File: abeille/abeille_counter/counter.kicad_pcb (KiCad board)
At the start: 2 copper layers, 3 parts, among them IC1 ATMEGA328-P

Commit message: start placing counter components
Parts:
- removed D1: LED, LEDs:LED-3MM
- removed IC1: ATMEGA328-P, Housings_DIP:DIP-28_W7.62mm_LongPads
- added P1: HE10-10, Connect:IDC_Header_Straight_10pins, B.Cu at (73.7, 108.0)
- added P2: HE10-10, Connect:IDC_Header_Straight_10pins, B.Cu at (212.1, 108.0)
- added R10: 100K, Resistors_SMD:R_1206_HandSoldering, F.Cu at (63.5, -96.5)
- added R11: 100K, Resistors_SMD:R_1206_HandSoldering, F.Cu at (63.5, -109.2)
- added R12: 100K, Resistors_SMD:R_1206_HandSoldering, F.Cu at (62.2, -123.2)
- added R13: 1K, Resistors_SMD:R_1206_HandSoldering, F.Cu at (62.2, -134.6)
- added R14: 1K, Resistors_SMD:R_1206_HandSoldering, F.Cu at (62.2, -144.8)
- added R15: 1K, Resistors_SMD:R_1206_HandSoldering, F.Cu at (174.0, 114.3)
- added R16: 1K, Resistors_SMD:R_1206_HandSoldering, F.Cu at (166.4, 114.3)
- added R17: 1K, Resistors_SMD:R_1206_HandSoldering, F.Cu at (110.5, 92.7)
- added R18: 1K, Resistors_SMD:R_1206_HandSoldering, F.Cu at (108.0, 114.3)
- added R19: 1K, Resistors_SMD:R_1206_HandSoldering, F.Cu at (94.0, -101.6)
- added R2: 1K, Resistors_SMD:R_1206_HandSoldering, F.Cu at (83.8, 113.0)
- added R20: 1K, Resistors_SMD:R_1206_HandSoldering, F.Cu at (94.0, -115.6)
- added R21: 100K, Resistors_SMD:R_1206_HandSoldering, F.Cu at (95.2, -128.3)
- added R22: 100K, Resistors_SMD:R_1206_HandSoldering, F.Cu at (95.2, -143.5)
- added R23: 100K, Resistors_SMD:R_1206_HandSoldering, F.Cu at (124.5, -143.5)
- added R24: 100K, Resistors_SMD:R_1206_HandSoldering, F.Cu at (124.5, -128.3)
- added R25: 1K, Resistors_SMD:R_1206_HandSoldering, F.Cu at (125.7, -115.6)
- added R26: 1K, Resistors_SMD:R_1206_HandSoldering, F.Cu at (127.0, -100.3)
- added R27: 1K, Resistors_SMD:R_1206_HandSoldering, F.Cu at (127.0, -87.6)
- added R28: 1K, Resistors_SMD:R_1206_HandSoldering, F.Cu at (127.0, -74.9)
- added R29: 1K, Resistors_SMD:R_1206_HandSoldering, F.Cu at (128.3, 91.4)
- added R3: 1K, Resistors_SMD:R_1206_HandSoldering, F.Cu at (95.2, -59.7)
- added R30: 1K, Resistors_SMD:R_1206_HandSoldering, F.Cu at (127.0, 114.3)
- added R31: 1K, Resistors_SMD:R_1206_HandSoldering, F.Cu at (194.3, 92.7)
- added R32: 1K, Resistors_SMD:R_1206_HandSoldering, F.Cu at (194.3, 113.0)
- added R33: 100K, Resistors_SMD:R_1206_HandSoldering, F.Cu at (149.9, -143.5)
- added R34: 100K, Resistors_SMD:R_1206_HandSoldering, F.Cu at (149.9, -127.0)
- added R35: 100K, Resistors_SMD:R_1206_HandSoldering, F.Cu at (149.9, -113.0)
- added R36: 100K, Resistors_SMD:R_1206_HandSoldering, F.Cu at (151.1, -97.8)
- added R37: 1K, Resistors_SMD:R_1206_HandSoldering, F.Cu at (152.4, -82.5)
- added R38: 1K, Resistors_SMD:R_1206_HandSoldering, F.Cu at (152.4, -66.0)
- added R39: 1K, Resistors_SMD:R_1206_HandSoldering, F.Cu at (201.9, 92.7)
- added R4: 1K, Resistors_SMD:R_1206_HandSoldering, F.Cu at (95.2, -76.2)
- added R40: 1K, Resistors_SMD:R_1206_HandSoldering, F.Cu at (186.7, 113.0)
- added R41: 1K, Resistors_SMD:R_1206_HandSoldering, F.Cu at (143.5, 91.4)
- added R42: 1K, Resistors_SMD:R_1206_HandSoldering, F.Cu at (143.5, 114.3)
- added R43: 1K, Resistors_SMD:R_1206_HandSoldering, F.Cu at (171.4, -144.8)
- added R44: 1K, Resistors_SMD:R_1206_HandSoldering, F.Cu at (171.4, -127.0)
- added R45: 100K, Resistors_SMD:R_1206_HandSoldering, F.Cu at (172.7, -114.3)
- added R46: 100K, Resistors_SMD:R_1206_HandSoldering, F.Cu at (172.7, -99.1)
- added R47: 100K, Resistors_SMD:R_1206_HandSoldering, F.Cu at (172.7, -83.8)
- added R48: 100K, Resistors_SMD:R_1206_HandSoldering, F.Cu at (172.7, -66.0)
- added R49: 0, Resistors_SMD:R_1206_HandSoldering, B.Cu at (86.4, 87.6)
- added R5: 1K, Resistors_SMD:R_1206_HandSoldering, F.Cu at (92.7, -90.2)
- added R50: 0, Resistors_SMD:R_1206_HandSoldering, B.Cu at (81.3, 87.6)
- added R51: 0, Resistors_SMD:R_1206_HandSoldering, B.Cu at (76.2, 87.6)
- added R52: 0, Resistors_SMD:R_1206_HandSoldering, B.Cu at (217.2, 120.7)
- added R53: 0, Resistors_SMD:R_1206_HandSoldering, F.Cu at (195.6, -143.5)
- added R54: 0, Resistors_SMD:R_1206_HandSoldering, F.Cu at (195.6, -128.3)
- added R55: 0, Resistors_SMD:R_1206_HandSoldering, F.Cu at (196.8, -114.3)
- added R56: 0, Resistors_SMD:R_1206_HandSoldering, F.Cu at (195.6, -100.3)
- added R57: 0, Resistors_SMD:R_1206_HandSoldering, F.Cu at (196.8, -82.5)
- added R6: 1K, Resistors_SMD:R_1206_HandSoldering, F.Cu at (61.0, -47.0)
- added R7: 1K, Resistors_SMD:R_1206_HandSoldering, F.Cu at (61.0, -58.4)
- added R8: 1K, Resistors_SMD:R_1206_HandSoldering, F.Cu at (63.5, -69.8)
- added R9: 100K, Resistors_SMD:R_1206_HandSoldering, F.Cu at (63.5, -83.8)
- added U1: IN_0, counter_footprint:ITR9608_DIP-4_0_ELL, F.Cu at (86.4, 99.1)
- added U10: OUT_2, counter_footprint:ITR9608_DIP-4_0_ELL, F.Cu at (119.4, 106.7)
- added U11: IN_6, counter_footprint:ITR9608_DIP-4_0_ELL, F.Cu at (185.4, 99.1)
- added U12: OUT_6, counter_footprint:ITR9608_DIP-4_0_ELL, F.Cu at (185.4, 106.7)
- added U13: IN_3, counter_footprint:ITR9608_DIP-4_0_ELL, F.Cu at (135.9, 99.1)
- added U14: OUT_3, counter_footprint:ITR9608_DIP-4_0_ELL, F.Cu at (135.9, 106.7)
- added U15: IN_7, counter_footprint:ITR9608_DIP-4_0_ELL, F.Cu at (201.9, 99.1)
- added U16: OUT_7, counter_footprint:ITR9608_DIP-4_0_ELL, F.Cu at (201.9, 106.7)
- added U17: pca9555, Housings_DIP:DIP-24_W15.24mm_LongPads, B.Cu at (130.8, 95.2)
- added U2: OUT_0, counter_footprint:ITR9608_DIP-4_0_ELL, F.Cu at (86.4, 106.7)
- added U3: IN_4, counter_footprint:ITR9608_DIP-4_0_ELL, F.Cu at (152.4, 99.1)
- added U4: OUT_4, counter_footprint:ITR9608_DIP-4_0_ELL, F.Cu at (152.4, 106.7)
- added U5: IN_1, counter_footprint:ITR9608_DIP-4_0_ELL, F.Cu at (102.9, 99.1)
- added U6: OUT_1, counter_footprint:ITR9608_DIP-4_0_ELL, F.Cu at (102.9, 106.7)
- added U7: IN_5, counter_footprint:ITR9608_DIP-4_0_ELL, F.Cu at (168.9, 99.1)
- added U8: OUT_5, counter_footprint:ITR9608_DIP-4_0_ELL, F.Cu at (168.9, 106.7)
- added U9: IN_2, counter_footprint:ITR9608_DIP-4_0_ELL, F.Cu at (119.4, 99.1)
- R1: value 1000 -> 1K; footprint Resistors_ThroughHole:Resistor_Horizontal_RM10mm -> Resistors_SMD:R_1206_HandSoldering
- moved R1 199.0 mm to (198.1, -64.8), turned to 0 degrees
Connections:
- R1 pad 1: Net-(IC1-Pad16) -> +5V
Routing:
- net GND: track 38.9 -> 0.00 mm
- net Net-(IC1-Pad16): track 30.8 -> 0.00 mm
- net +5V: track 16.3 -> 0.00 mm
- net Net-(R1-Pad2): track 3.81 -> 0.00 mm

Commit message: start placing of resistor of abeille_counter
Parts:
- R53, R54, R55, R56, R57: moved to B.Cu
- moved R14 260.7 mm to (91.4, 114.3), turned to 90 degrees
- moved R12 259.9 mm to (158.8, 118.1)
- moved R23 259.3 mm to (96.5, 114.3), turned to 90 degrees
- moved R24 249.1 mm to (151.1, 119.4)
- moved R22 243.8 mm to (172.7, 87.6)
- moved R44 243.7 mm to (205.7, 114.3), turned to 270 degrees
- moved R20 242.2 mm to (170.2, 114.3), turned to 270 degrees
- moved R43 235.7 mm to (201.9, 88.9), turned to 180 degrees
- moved R53 232.5 mm to (221.0, 87.6), turned to 90 degrees
- moved R33 231.0 mm to (127.0, 86.4)
- moved R13 229.2 mm to (118.1, 87.6), turned to 180 degrees
- moved R56 227.7 mm to (208.3, 127.0), turned to 90 degrees
- moved R11 224.7 mm to (86.4, 114.3), turned to 90 degrees
- moved R21 221.1 mm to (102.9, 92.7)
- moved R34 220.4 mm to (194.3, 88.9)
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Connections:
- P1 pad 10: /5V -> +5V
- P1 pad 9: /5V -> +5V
- P2 pad 10: /5V -> +5V
- P2 pad 9: /5V -> +5V
- R52 pad 1: Net-(R52-Pad1) -> GND
- R53 pad 2: Net-(R53-Pad2) -> +5V
- R54 pad 1: Net-(R54-Pad1) -> GND
- R55 pad 2: Net-(R55-Pad2) -> +5V
- R56 pad 1: Net-(R56-Pad1) -> GND
- R57 pad 2: Net-(R57-Pad2) -> +5V
- U17 pad 24: /5V -> +5V

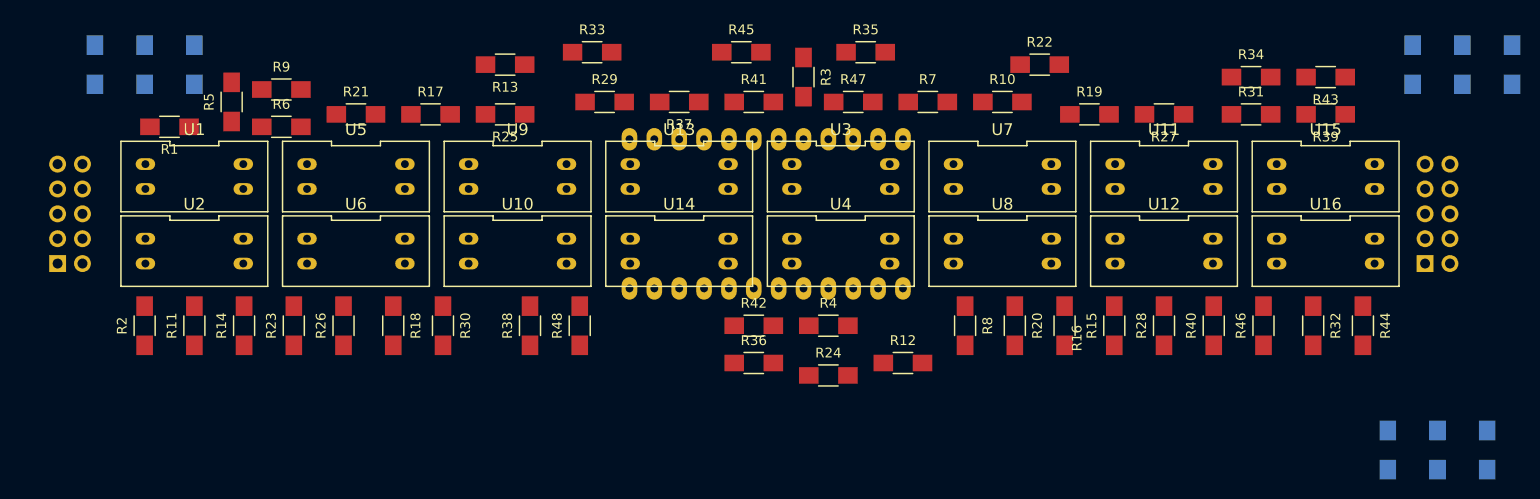
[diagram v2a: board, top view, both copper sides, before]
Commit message: first final routing version of abeille counter
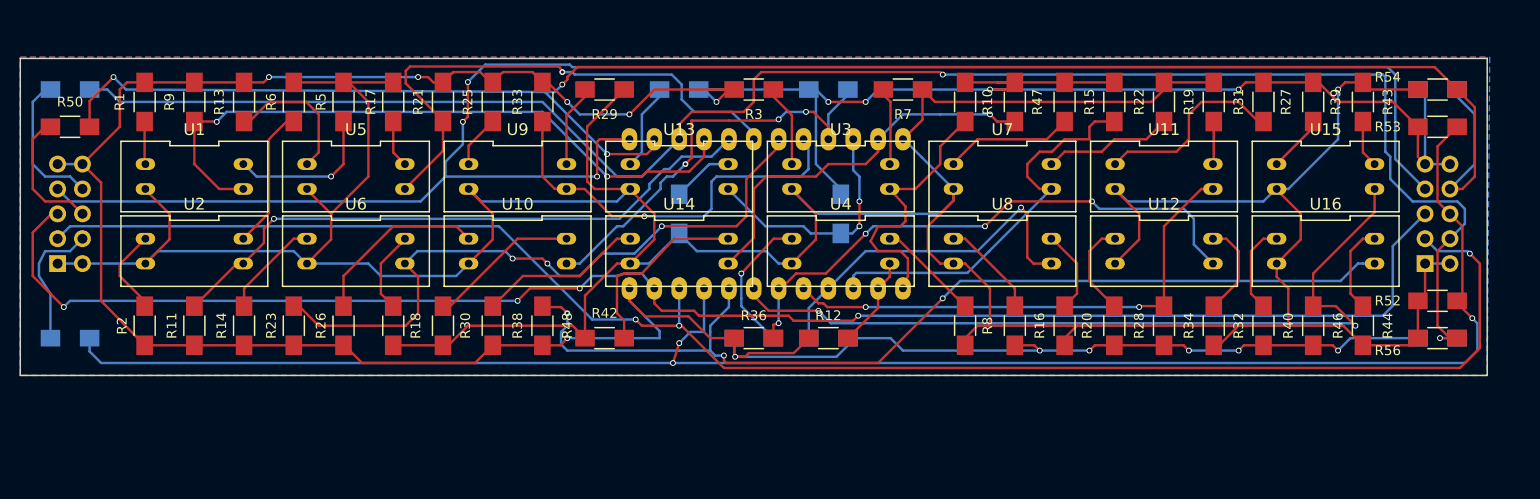
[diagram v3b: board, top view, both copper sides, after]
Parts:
- R24, R35, R37, R4, R41, R45: moved to B.Cu
- R50, R52, R53, R54, R56: moved to F.Cu
- moved R49 30.7 mm to (73.7, 115.6), turned to 180 degrees
- moved R13 26.9 mm to (91.4, 91.4), turned to 270 degrees
- moved R34 26.9 mm to (185.4, 114.3), turned to 90 degrees
- moved R15 23.4 mm to (175.3, 91.4), turned to 270 degrees
- moved R45 19.4 mm to (152.4, 102.9), turned to 270 degrees
- moved R47 16.5 mm to (170.2, 91.4), turned to 270 degrees
- moved R52 16.1 mm to (213.4, 111.8), turned to 0 degrees
- moved R42 15.3 mm to (128.3, 115.6), turned to 180 degrees
- moved R41 13.7 mm to (135.9, 102.9), turned to 270 degrees
- moved R56 12.5 mm to (213.4, 115.6), turned to 0 degrees
- moved R57 11.4 mm to (213.4, 115.6), turned to 180 degrees
- moved R5 11.4 mm to (101.6, 91.4)
- moved R27 10.2 mm to (195.6, 91.4), turned to 270 degrees
- moved R32 10.2 mm to (190.5, 114.3)
- moved R50 9.92 mm to (73.7, 94.0), turned to 180 degrees
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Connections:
- R10 pad 2: Net-(R10-Pad2) -> /D8
- R21 pad 2: Net-(R21-Pad2) -> /D2
- R22 pad 2: Net-(R22-Pad2) -> /D10
- R33 pad 2: Net-(R33-Pad2) -> /D4
- R34 pad 2: Net-(R34-Pad2) -> /D12
- R45 pad 2: Net-(R45-Pad2) -> /D6
- R46 pad 2: Net-(R46-Pad2) -> /D14
- R9 pad 2: Net-(R9-Pad2) -> /D0
- U1 pad 3: Net-(R9-Pad2) -> /D0
- U11 pad 3: Net-(R34-Pad2) -> /D12
- U13 pad 3: Net-(R45-Pad2) -> /D6
- U15 pad 3: Net-(R46-Pad2) -> /D14
- U3 pad 3: Net-(R10-Pad2) -> /D8
- U5 pad 3: Net-(R21-Pad2) -> /D2
- U7 pad 3: Net-(R22-Pad2) -> /D10
- U9 pad 3: Net-(R33-Pad2) -> /D4
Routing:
- net GND: track 0.00 -> 418.8 mm, vias 0 -> 1
- net +5V: track 0.00 -> 391.9 mm, vias 0 -> 16
- net /A1: track 0.00 -> 185.6 mm, vias 0 -> 3
- net /INT#: track 0.00 -> 183.1 mm, vias 0 -> 3
- net /A2: track 0.00 -> 182.1 mm, vias 0 -> 2
- net /A0: track 0.00 -> 179.5 mm, vias 0 -> 3
- net /SCL: track 0.00 -> 171.7 mm, vias 0 -> 3
- net /SDA: track 0.00 -> 163.8 mm, vias 0 -> 4
- net /D15: track 0.00 -> 101.9 mm, vias 0 -> 3
- net /D14: track 0.00 -> 83.2 mm, vias 0 -> 2
- net /D0: track 0.00 -> 68.3 mm, vias 0 -> 2
- net /D3: track 0.00 -> 67.9 mm, vias 0 -> 3
- net /D1: track 0.00 -> 62.8 mm, vias 0 -> 1
- net /D13: track 0.00 -> 57.7 mm, vias 0 -> 4
- net /D2: track 0.00 -> 55.4 mm, vias 0 -> 1
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- added copper zone on B.Cu, net GND
- added copper zone on F.Cu, net GND
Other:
- board outline added: 149.9 x 32.4 mm
- net class Large added: clearance 0.5, trace_width 0.5, via_dia 1, via_drill 0.6
